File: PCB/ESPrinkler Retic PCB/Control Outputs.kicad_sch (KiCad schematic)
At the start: 126 parts, among them Q10 AO3400A, Q11 AO3400A, Q3 AO3400A, Q4 AO3400A, Q5 AO3400A, Q6 AO3400A, Q7 AO3400A, Q8 AO3400A, Q9 AO3400A, U10 MOC3063S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

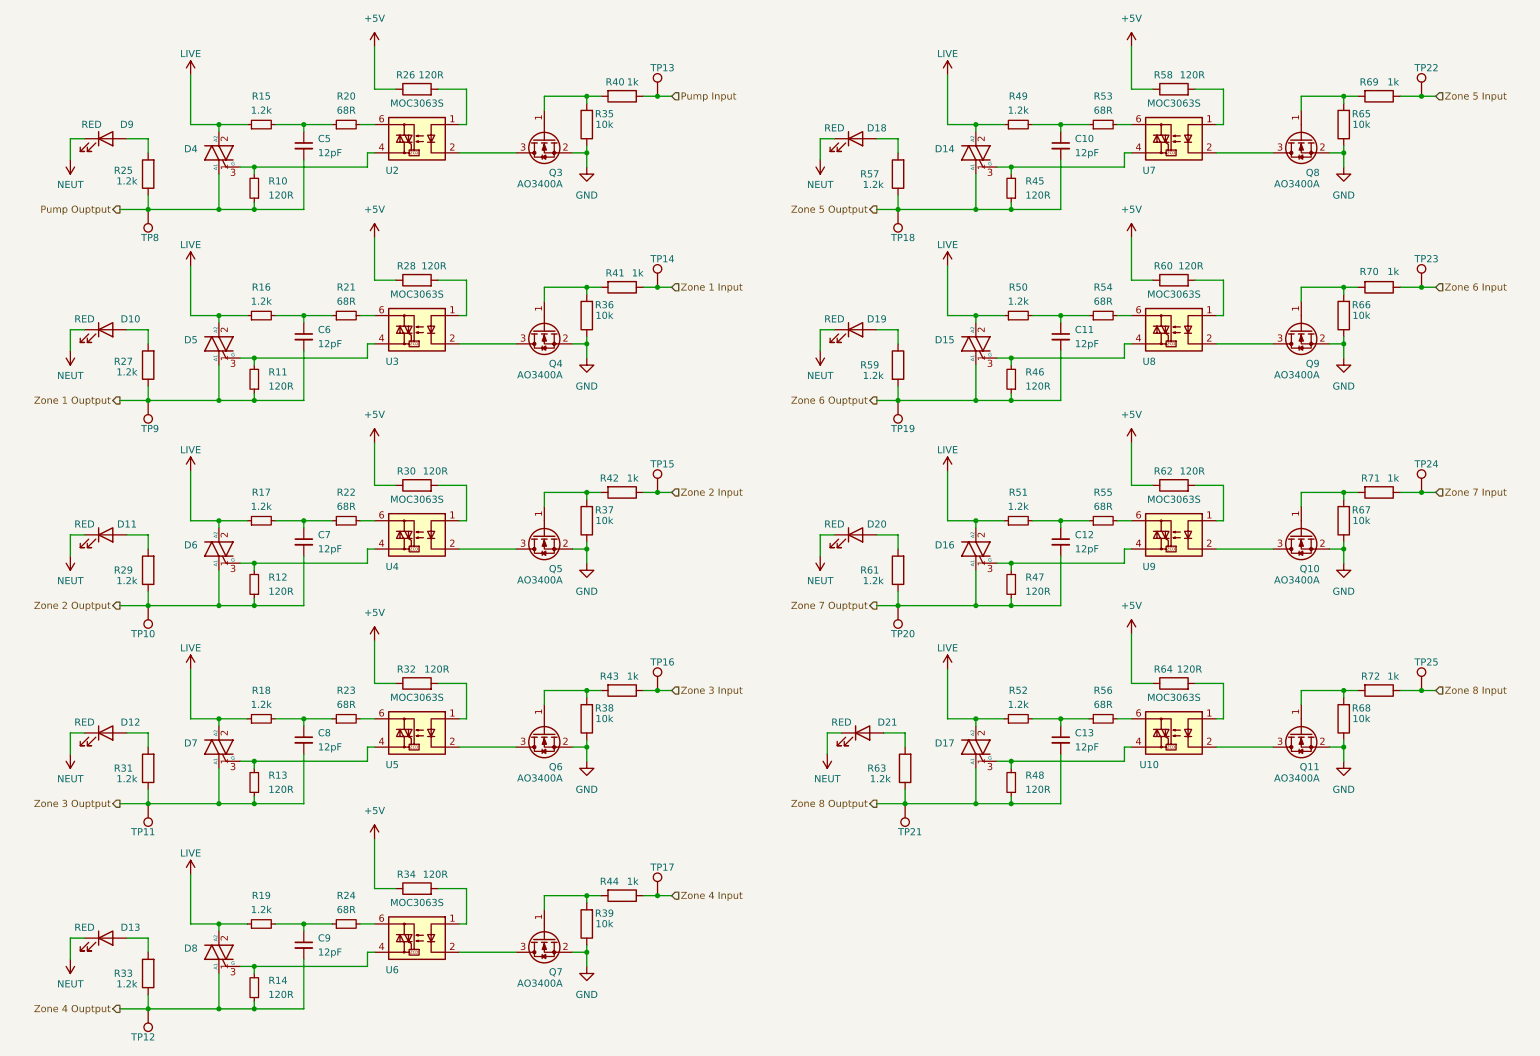
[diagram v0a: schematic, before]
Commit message: Continue PCB layout
Final placements and traces of components for first revision.
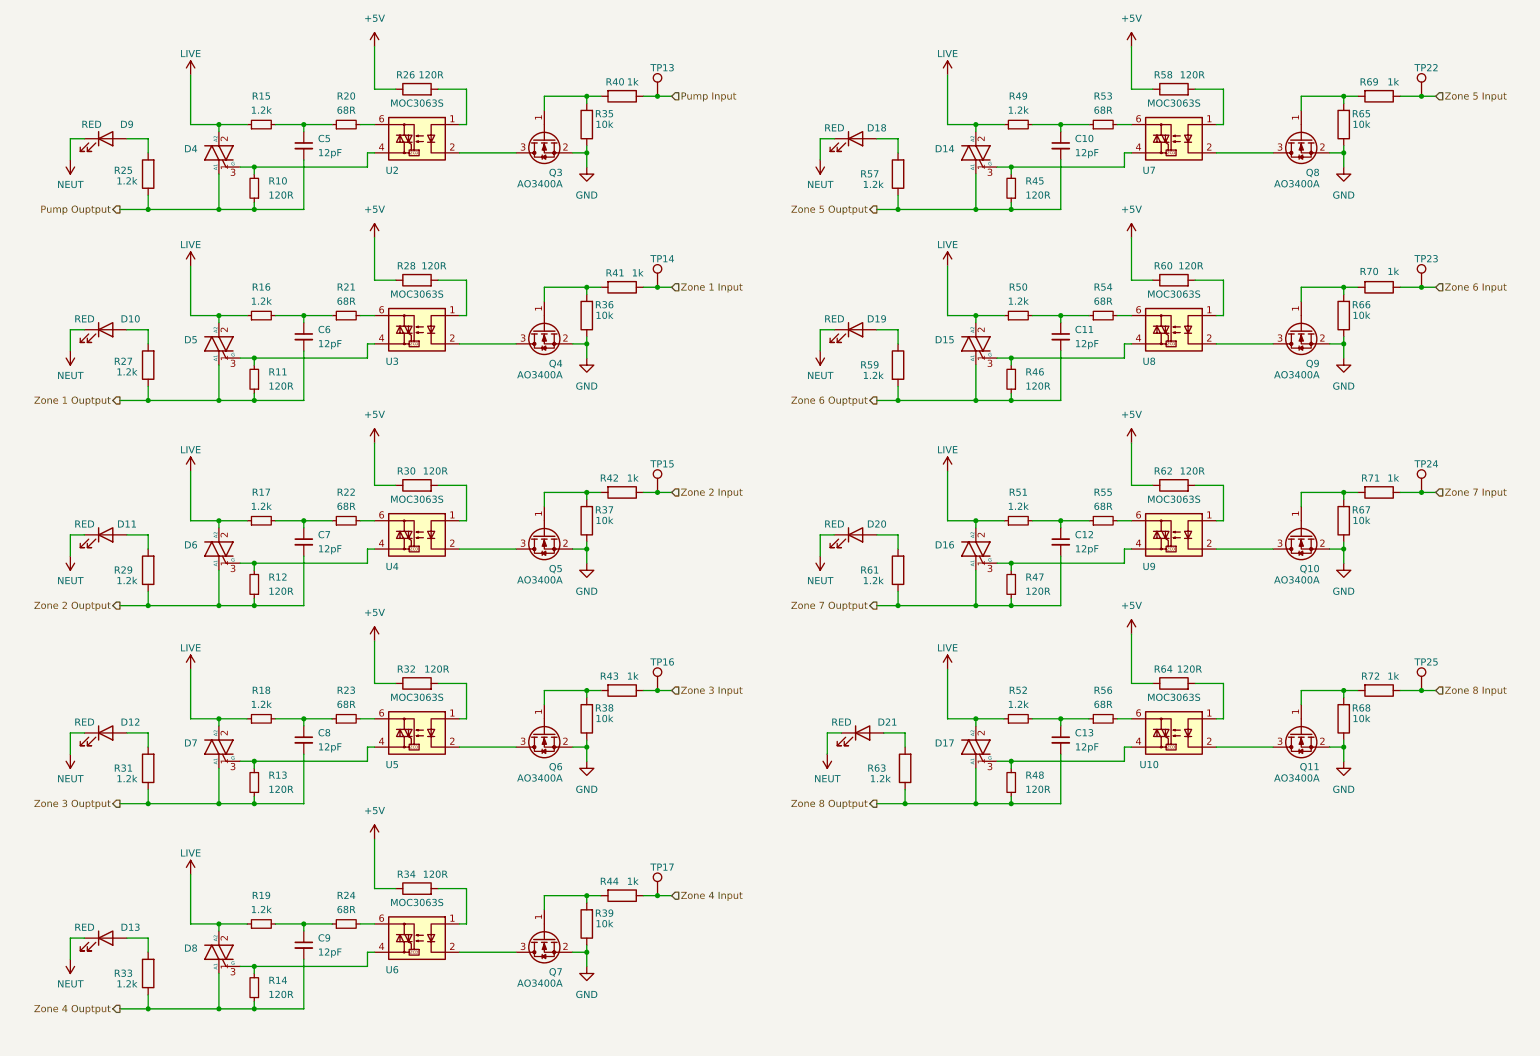
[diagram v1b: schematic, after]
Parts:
- removed TP10, TP11, TP12, TP18, TP19, TP20, TP21, TP8, TP9: TestPoint, TestPoint:TestPoint_Pad_D1.5mm, symbol Connector:TestPoint

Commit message: Update Schematics
For all, update title block information.

Power IO:
- Change PTC fuse footprint reference
- Add part info for J1

Control Outputs:
- Add notes and box areas of schematic for clarity
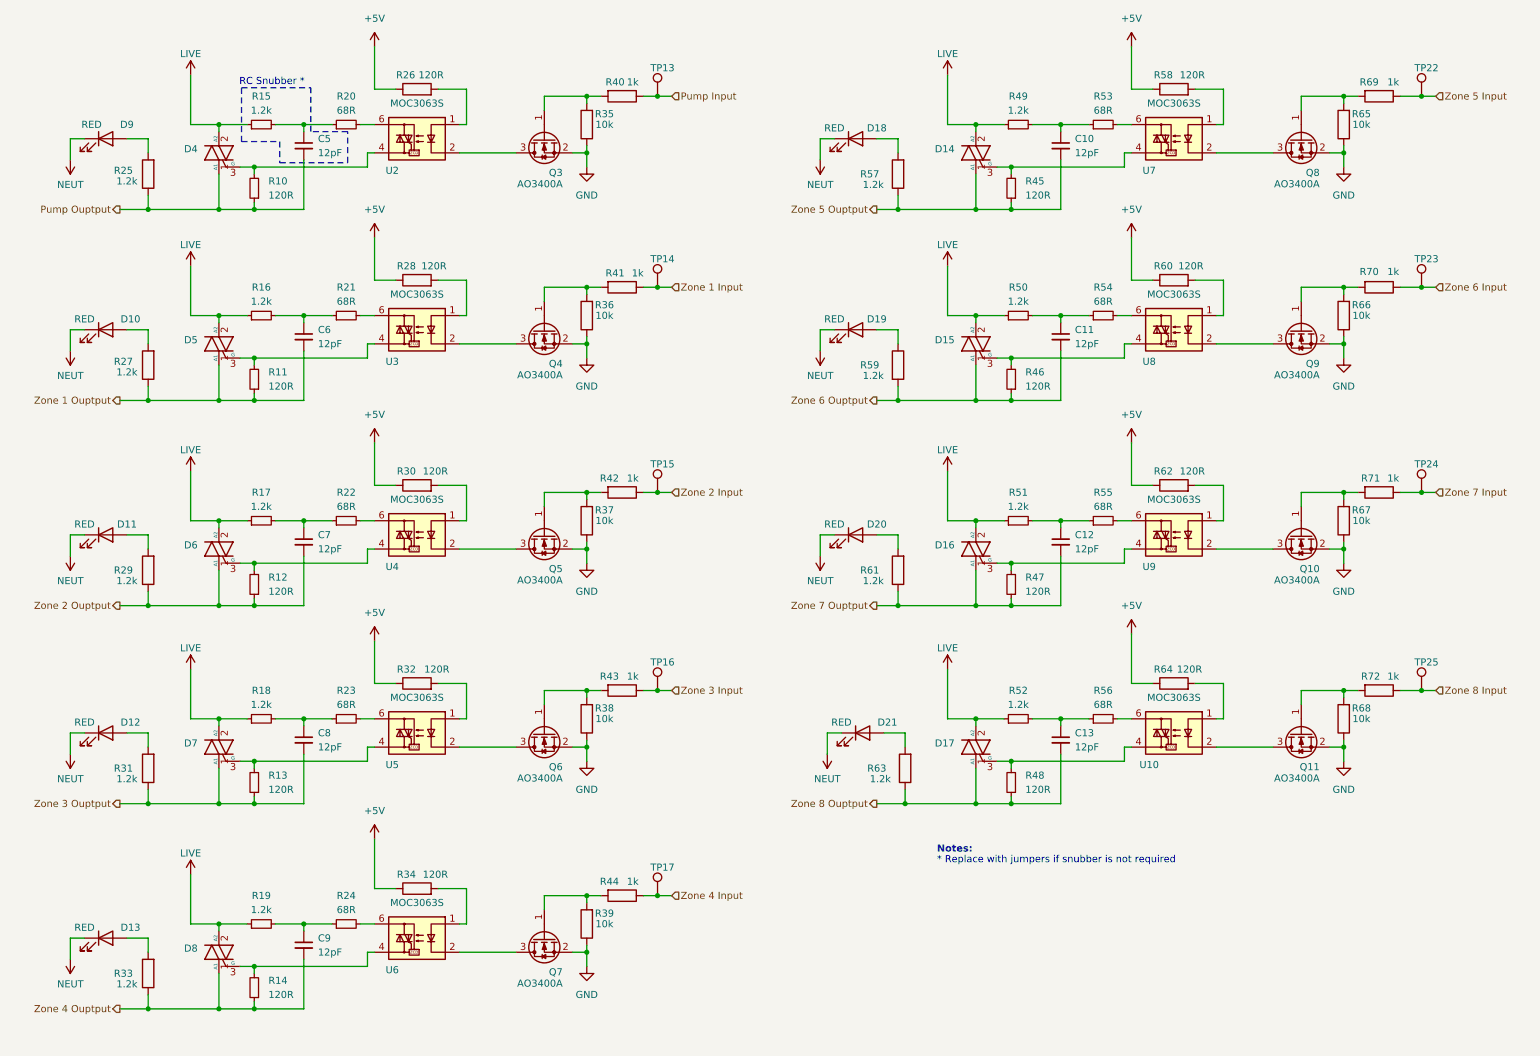
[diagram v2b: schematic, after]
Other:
- note added: "* Replace with jumpers if snubber is not required"
- note added: "Notes:"
- note added: "RC Snubber *"
- title: (none) -> ESPrinkler Retic Controller
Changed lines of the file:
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@@
 	(generator_version "9.0")
 	(paper "A4")
+	(title_block
+		(title "ESPrinkler Retic Controller")
+		(date "2025-06-01")
+		(rev "1.0")
+	)
+	(text "Notes:"
+		(exclude_from_sim no)
+		(at 177.165 163.195 0)
+		(effects
+			(font
+				(size 1.27 1.27)
+				(thickness 0.254)
+				(bold yes)
+			)
+			(justify left)
+		)
+	)
+	(text "RC Snubber *"
+		(exclude_from_sim no)
+		(at 57.785 25.4 0)
+		(effects
+			(font
+				(size 1.27 1.27)
+			)
+		)
+	)
+	(text "* Replace with jumpers if snubber is not required"
+		(exclude_from_sim no)
+		(at 177.165 165.1 0)
+		(effects
+			(font
+				(size 1.27 1.27)
+				(thickness 0.1588)
+			)
+			(justify left)
+		)
+	)
 	(junction
 		(at 35.56 191.77)
@@
 		)
 	)
+	(polyline
+		(pts
+			(xy 52.324 36.068) (xy 59.182 36.068)
+		)
+		(stroke
+			(width 0)
+			(type dash)
+		)
+	)
 	(wire
 		(pts
@@
 		)
 	)
+	(polyline
+		(pts
+			(xy 64.77 34.29) (xy 64.77 26.416)
+		)
+		(stroke
+			(width 0)
+			(type dash)
+		)
+	)
 	(wire
 		(pts
@@
 		)
 	)
+	(polyline
+		(pts
+			(xy 59.182 39.878) (xy 71.374 39.878)
+		)
+		(stroke
+			(width 0)
+			(type dash)
+		)
+	)
 	(wire
 		(pts
@@
 		(stroke
 			(width 0)
-			(type default)
+			(type dash)
 		)
 	)
@@
 		)
 	)
+	(polyline
+		(pts
+			(xy 71.374 39.878) (xy 71.374 34.29)
+		)
+		(stroke
+			(width 0)
+			(type dash)
+		)
+	)
 	(wire
 		(pts
@@
 		)
 	)
+	(polyline
+		(pts
+			(xy 59.182 36.068) (xy 59.182 39.878)
+		)
+		(stroke
+			(width 0)
+			(type dash)
+		)
+	)
 	(wire
 		(pts
@@
 		)
 	)
+	(polyline
+		(pts
+			(xy 52.324 26.416) (xy 52.324 36.068)
+		)
+		(stroke
+			(width 0)
+			(type dash)
+		)
+	)
 	(wire
 		(pts
@@
 		)
 	)
+	(polyline
+		(pts
+			(xy 52.324 26.416) (xy 64.77 26.416)
+		)
+		(stroke
+			(width 0)
+			(type dash)
+		)
+	)
 	(wire
 		(pts
@@
 		)
 	)
+	(polyline
+		(pts
+			(xy 71.374 34.29) (xy 64.77 34.29)
+		)
+		(stroke
+			(width 0)
+			(type dash)
+		)
+	)

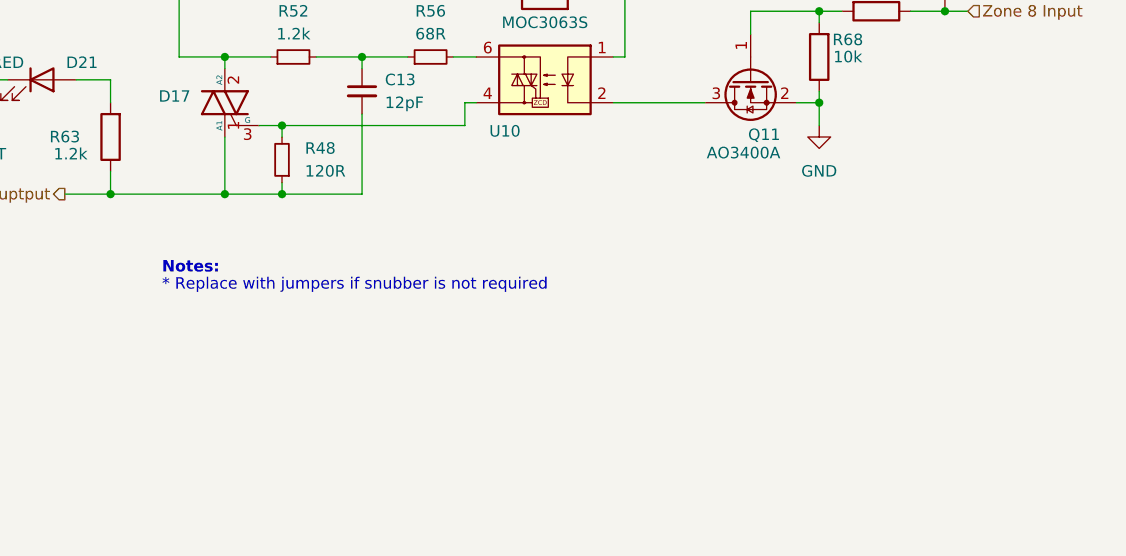
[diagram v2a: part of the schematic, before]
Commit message: Adjust notes on SCH
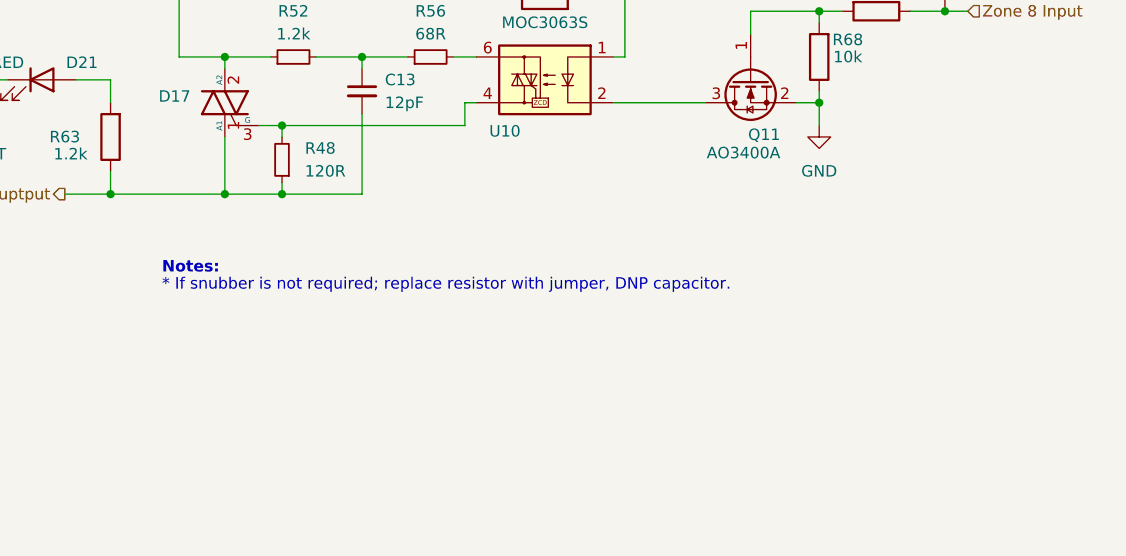
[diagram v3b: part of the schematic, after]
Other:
- note added: "* If snubber is not required; replace resistor with jumper, DNP capacitor."
- note removed: "* Replace with jumpers if snubber is not required"
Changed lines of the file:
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@@
 		)
 	)
-	(text "* Replace with jumpers if snubber is not required"
+	(text "* If snubber is not required; replace resistor with jumper, DNP capacitor."
 		(exclude_from_sim no)
 		(at 177.165 165.1 0)

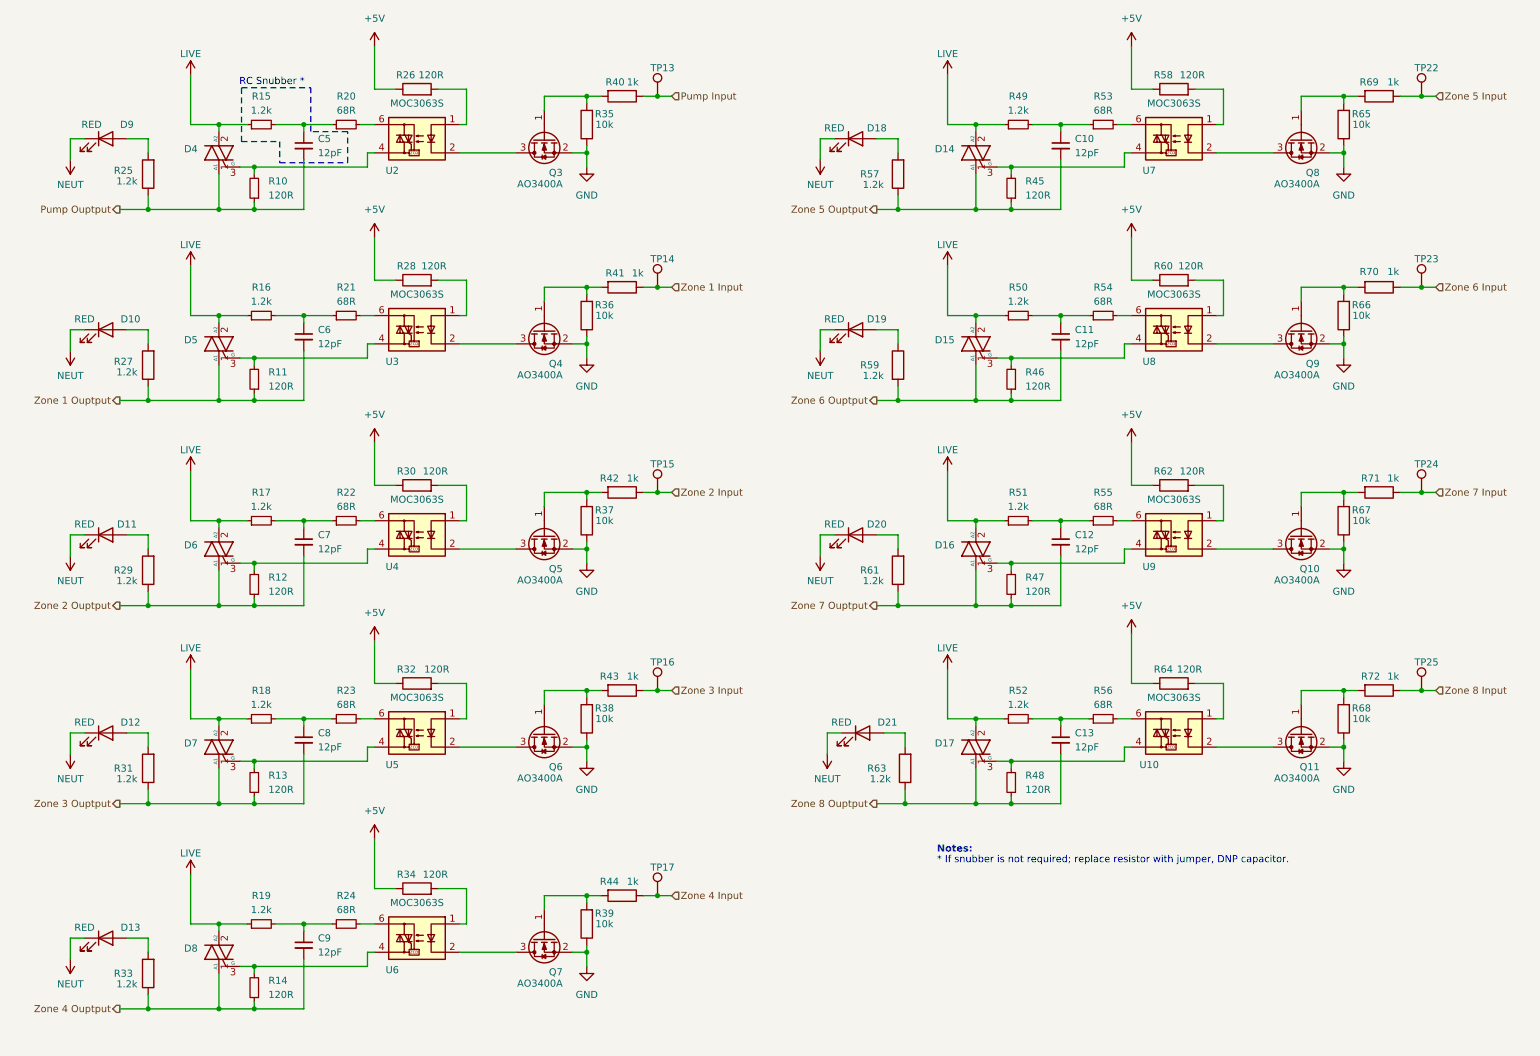
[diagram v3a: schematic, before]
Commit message: Prepare for V1.0 production
Export fab files for PCB manufacturing and parts ordering
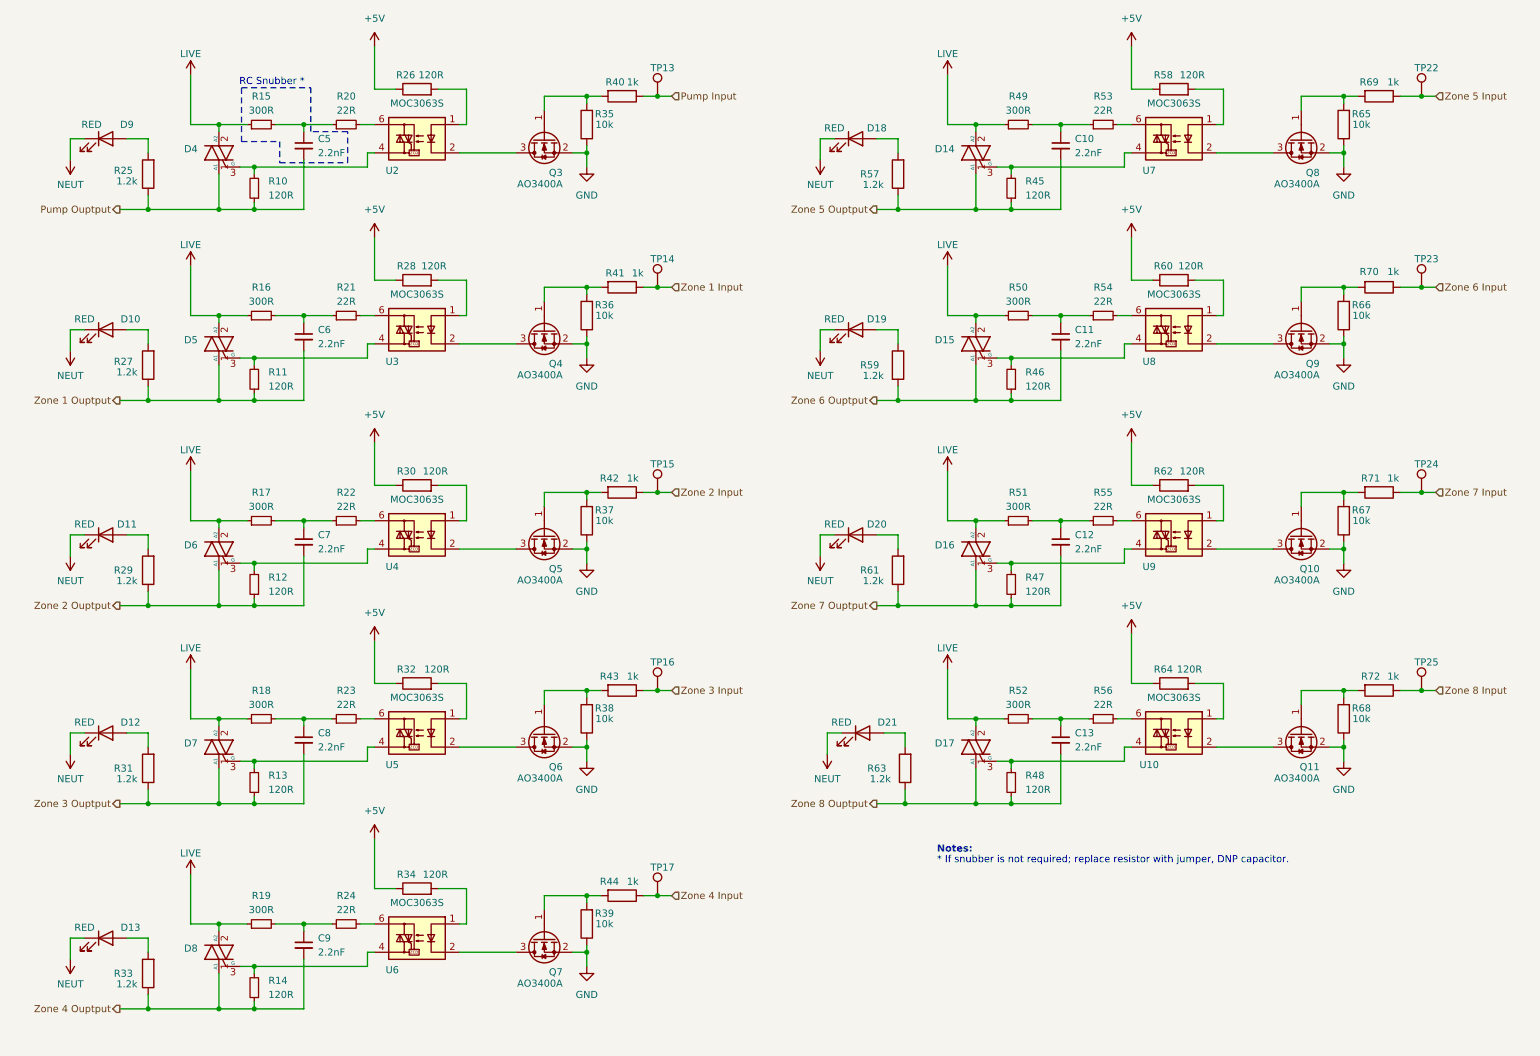
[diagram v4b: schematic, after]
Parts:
- C10, C11, C12, C13, C5, C6, C7, C8, C9: value 12pF -> 2.2nF; Manufacturer P/N CL10C120JB8NNNC -> CL21C222JBFNNNE; Supplier P/N C38523 -> C28260
- R15, R16, R17, R18, R19, R49, R50, R51, R52: value 1.2k -> 300R; Manufacturer P/N 0805W8F1201T5E -> 0805W8F3000T5E; Supplier P/N C17379 -> C17617
- R20, R21, R22, R23, R24, R53, R54, R55, R56: value 68R -> 22R; Manufacturer P/N 0805W8F680JT5E -> 0805W8F220JT5E; Supplier P/N C17802 -> C17561
